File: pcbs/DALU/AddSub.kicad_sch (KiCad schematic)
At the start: 14 parts, among them U401 74HC86, U402 74HC08, U403 74HC86, U404 74HC86, U405 74HC283, U406 74HC283, U407 74HC245, U408 74HC245

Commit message: More rerouting
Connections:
- net RESULT7: now reaches U407.11 (B7)
- net RESULT6: now reaches U407.12 (B6)
- net RESULT5: now reaches U407.13 (B5)
- net RESULT4: now reaches U407.14 (B4)
- net RESULT3: now reaches U407.15 (B3)
- net RESULT2: now reaches U407.16 (B2)
- net RESULT1: now reaches U407.17 (B1)
- net RESULT0: now reaches U407.18 (B0)
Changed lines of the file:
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@@
+    (stroke (width 0) (type default) (color 0 0 0 0))
+  )
+  (bus_entry (at 254.635 43.18) (size -2.54 2.54)
     (stroke (width 0) (type default) (color 0 0 0 0))
   )
@@
     (stroke (width 0) (type default) (color 0 0 0 0))
   )
+  (bus_entry (at 254.635 50.8) (size -2.54 2.54)
+    (stroke (width 0) (type default) (color 0 0 0 0))
+  )
   (bus_entry (at 100.33 144.78) (size -2.54 2.54)
     (stroke (width 0) (type default) (color 0 0 0 0))
@@
     (stroke (width 0) (type default) (color 0 0 0 0))
   )
+  (bus_entry (at 254.635 55.88) (size -2.54 2.54)
+    (stroke (width 0) (type default) (color 0 0 0 0))
+  )
+  (bus_entry (at 254.635 45.72) (size -2.54 2.54)
+    (stroke (width 0) (type default) (color 0 0 0 0))
+  )
   (bus_entry (at 64.77 49.53) (size 2.54 2.54)
     (stroke (width 0) (type default) (color 0 0 0 0))
   )
+  (bus_entry (at 254.635 58.42) (size -2.54 2.54)
+    (stroke (width 0) (type default) (color 0 0 0 0))
+  )
   (bus_entry (at 64.77 96.52) (size 2.54 2.54)
     (stroke (width 0) (type default) (color 0 0 0 0))
@@
     (stroke (width 0) (type default) (color 0 0 0 0))
   )
+  (bus_entry (at 254.635 48.26) (size -2.54 2.54)
+    (stroke (width 0) (type default) (color 0 0 0 0))
+  )
   (bus_entry (at 100.33 114.3) (size -2.54 2.54)
     (stroke (width 0) (type default) (color 0 0 0 0))
@@
     (stroke (width 0) (type default) (color 0 0 0 0))
   )
+  (bus_entry (at 254.635 60.96) (size -2.54 2.54)
+    (stroke (width 0) (type default) (color 0 0 0 0))
+  )
   (bus_entry (at 134.62 63.5) (size 2.54 2.54)
     (stroke (width 0) (type default) (color 0 0 0 0))
@@
     (stroke (width 0) (type default) (color 0 0 0 0))
   )
+  (bus_entry (at 254.635 53.34) (size -2.54 2.54)
+    (stroke (width 0) (type default) (color 0 0 0 0))
+  )
   (bus_entry (at 143.51 55.88) (size 2.54 2.54)
     (stroke (width 0) (type default) (color 0 0 0 0))
@@
     (stroke (width 0) (type default) (color 0 0 0 0))
   )
+  (bus (pts (xy 254.635 36.83) (xy 254.635 43.18))
+    (stroke (width 0) (type default) (color 0 0 0 0))
+  )
   (wire (pts (xy 60.96 63.5) (xy 60.96 72.39))
     (stroke (width 0) (type default) (color 0 0 0 0))
@@
     (stroke (width 0) (type default) (color 0 0 0 0))
   )
+  (bus (pts (xy 254.635 43.18) (xy 254.635 45.72))
+    (stroke (width 0) (type default) (color 0 0 0 0))
+  )
   (wire (pts (xy 137.16 120.65) (xy 156.21 120.65))
     (stroke (width 0) (type default) (color 0 0 0 0))
@@
     (stroke (width 0) (type default) (color 0 0 0 0))
   )
+  (bus (pts (xy 254.635 58.42) (xy 254.635 60.96))
+    (stroke (width 0) (type default) (color 0 0 0 0))
+  )
   (wire (pts (xy 193.675 146.685) (xy 193.675 149.86))
     (stroke (width 0) (type default) (color 0 0 0 0))
   )
+  (bus (pts (xy 261.62 36.83) (xy 254.635 36.83))
+    (stroke (width 0) (type default) (color 0 0 0 0))
+  )
   (wire (pts (xy 163.83 87.63) (xy 168.91 87.63))
     (stroke (width 0) (type default) (color 0 0 0 0))
@@
     (stroke (width 0) (type default) (color 0 0 0 0))
   )
+  (bus (pts (xy 254.635 50.8) (xy 254.635 53.34))
+    (stroke (width 0) (type default) (color 0 0 0 0))
+  )
   (wire (pts (xy 227.33 120.65) (xy 232.41 120.65))
     (stroke (width 0) (type default) (color 0 0 0 0))
@@
     (stroke (width 0) (type default) (color 0 0 0 0))
   )
+  (bus (pts (xy 254.635 48.26) (xy 254.635 50.8))
+    (stroke (width 0) (type default) (color 0 0 0 0))
+  )
   (wire (pts (xy 163.83 78.74) (xy 168.91 78.74))
     (stroke (width 0) (type default) (color 0 0 0 0))
@@
     (stroke (width 0) (type default) (color 0 0 0 0))
   )
+  (wire (pts (xy 238.76 50.8) (xy 252.095 50.8))
+    (stroke (width 0) (type default) (color 0 0 0 0))
+  )
   (bus (pts (xy 134.62 113.03) (xy 134.62 110.49))
     (stroke (width 0) (type default) (color 0 0 0 0))
@@
     (stroke (width 0) (type default) (color 0 0 0 0))
   )
+  (bus (pts (xy 254.635 45.72) (xy 254.635 48.26))
+    (stroke (width 0) (type default) (color 0 0 0 0))
+  )
   (wire (pts (xy 67.31 36.83) (xy 77.47 36.83))
     (stroke (width 0) (type default) (color 0 0 0 0))
@@
     (stroke (width 0) (type default) (color 0 0 0 0))
   )
+  (wire (pts (xy 238.76 58.42) (xy 252.095 58.42))
+    (stroke (width 0) (type default) (color 0 0 0 0))
+  )
   (bus (pts (xy 143.51 53.34) (xy 143.51 55.88))
     (stroke (width 0) (type default) (color 0 0 0 0))
   )
+  (wire (pts (xy 238.76 55.88) (xy 252.095 55.88))
+    (stroke (width 0) (type default) (color 0 0 0 0))
+  )
   (wire (pts (xy 77.47 134.62) (xy 60.96 134.62))
     (stroke (width 0) (type default) (color 0 0 0 0))
@@
     (stroke (width 0) (type default) (color 0 0 0 0))
   )
+  (bus (pts (xy 254.635 55.88) (xy 254.635 58.42))
+    (stroke (width 0) (type default) (color 0 0 0 0))
+  )
+  (wire (pts (xy 238.76 63.5) (xy 252.095 63.5))
+    (stroke (width 0) (type default) (color 0 0 0 0))
+  )
   (wire (pts (xy 168.91 35.56) (xy 168.91 38.1))
     (stroke (width 0) (type default) (color 0 0 0 0))
@@
     (stroke (width 0) (type default) (color 0 0 0 0))
   )
+  (wire (pts (xy 238.76 45.72) (xy 252.095 45.72))
+    (stroke (width 0) (type default) (color 0 0 0 0))
+  )
   (wire (pts (xy 67.31 67.31) (xy 77.47 67.31))
     (stroke (width 0) (type default) (color 0 0 0 0))
@@
     (stroke (width 0) (type default) (color 0 0 0 0))
   )
+  (wire (pts (xy 238.76 48.26) (xy 252.095 48.26))
+    (stroke (width 0) (type default) (color 0 0 0 0))
+  )
   (bus (pts (xy 134.62 115.57) (xy 134.62 113.03))
     (stroke (width 0) (type default) (color 0 0 0 0))
@@
     (stroke (width 0) (type default) (color 0 0 0 0))
   )
+  (bus (pts (xy 254.635 53.34) (xy 254.635 55.88))
+    (stroke (width 0) (type default) (color 0 0 0 0))
+  )
   (bus (pts (xy 134.62 110.49) (xy 134.62 68.58))
     (stroke (width 0) (type default) (color 0 0 0 0))
@@
     (stroke (width 0) (type default) (color 0 0 0 0))
   )
+  (wire (pts (xy 238.76 60.96) (xy 252.095 60.96))
+    (stroke (width 0) (type default) (color 0 0 0 0))
+  )
   (wire (pts (xy 146.05 50.8) (xy 156.21 50.8))
     (stroke (width 0) (type default) (color 0 0 0 0))
@@
   )
   (wire (pts (xy 77.47 72.39) (xy 60.96 72.39))
+    (stroke (width 0) (type default) (color 0 0 0 0))
+  )
+  (wire (pts (xy 238.76 53.34) (xy 252.095 53.34))
     (stroke (width 0) (type default) (color 0 0 0 0))
   )
@@
     (effects (font (size 1.27 1.27)) (justify left bottom))
   )
+  (label "RESULT4" (at 238.76 55.88 0)
+    (effects (font (size 1.27 1.27)) (justify left bottom))
+  )
+  (label "RESULT3" (at 238.76 53.34 0)
+    (effects (font (size 1.27 1.27)) (justify left bottom))
+  )
   (label "B'4" (at 137.16 113.03 0)
     (effects (font (size 1.27 1.27)) (justify left bottom))
@@
     (effects (font (size 1.27 1.27)) (justify left bottom))
   )
+  (label "RESULT2" (at 238.76 50.8 0)
+    (effects (font (size 1.27 1.27)) (justify left bottom))
+  )
+  (label "RESULT5" (at 238.76 58.42 0)
+    (effects (font (size 1.27 1.27)) (justify left bottom))
+  )
   (label "B'0" (at 92.71 39.37 0)
     (effects (font (size 1.27 1.27)) (justify left bottom))
@@
     (effects (font (size 1.27 1.27)) (justify left bottom))
   )
+  (label "RESULT6" (at 238.76 60.96 0)
+    (effects (font (size 1.27 1.27)) (justify left bottom))
+  )
   (label "A5" (at 146.05 102.87 0)
     (effects (font (size 1.27 1.27)) (justify left bottom))
   )
   (label "S_{1}" (at 182.88 48.26 0)
+    (effects (font (size 1.27 1.27)) (justify left bottom))
+  )
+  (label "RESULT0" (at 238.76 45.72 0)
     (effects (font (size 1.27 1.27)) (justify left bottom))
   )
@@
     (effects (font (size 1.27 1.27)) (justify left bottom))
   )
+  (label "RESULT1" (at 238.76 48.26 0)
+    (effects (font (size 1.27 1.27)) (justify left bottom))
+  )
   (label "A0" (at 146.685 50.8 0)
     (effects (font (size 1.27 1.27)) (justify left bottom))
@@
   )
   (label "B'0" (at 137.16 63.5 0)
+    (effects (font (size 1.27 1.27)) (justify left bottom))
+  )
+  (label "RESULT7" (at 238.76 63.5 0)
     (effects (font (size 1.27 1.27)) (justify left bottom))
   )
@@
     (effects (font (size 1.27 1.27)) (justify right))
   )
+  (hierarchical_label "RESULT[0..7]" (shape tri_state) (at 261.62 36.83 0)
+    (effects (font (size 1.27 1.27)) (justify left))
+  )
   (hierarchical_label "B[0..7]" (shape input) (at 45.72 29.21 180)

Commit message: Finish preliminary routing
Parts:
- added C407, C408: 100n, Capacitor_SMD:C_0603_1608Metric, symbol Device:C
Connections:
- net +5V: now also C407.1, C408.1
- net GND: now also C407.2, C408.2
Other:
- moved on the sheet: C401, C402, C403, C404, C405, C406

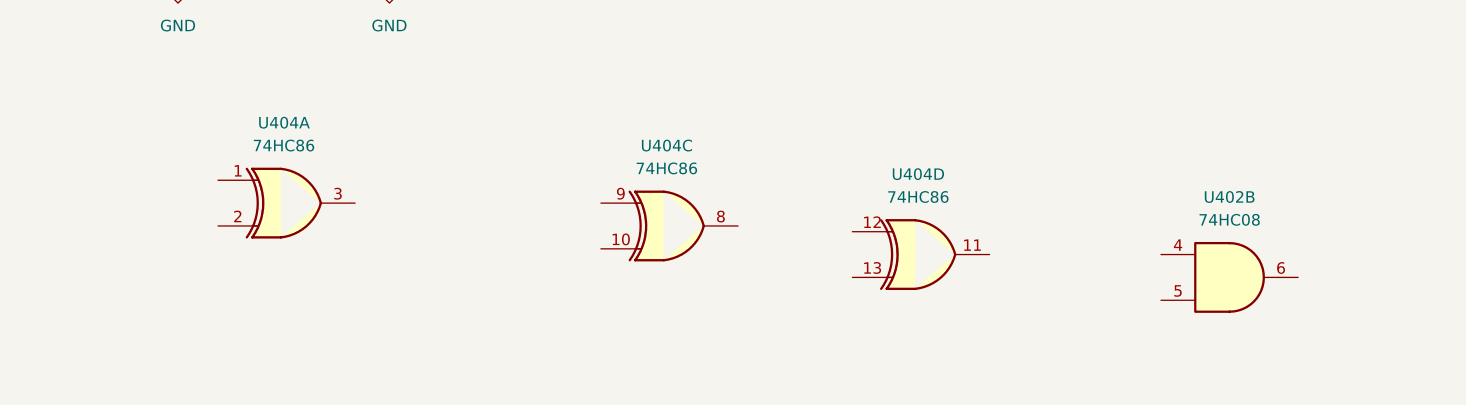
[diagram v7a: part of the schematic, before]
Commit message: Filling out connections
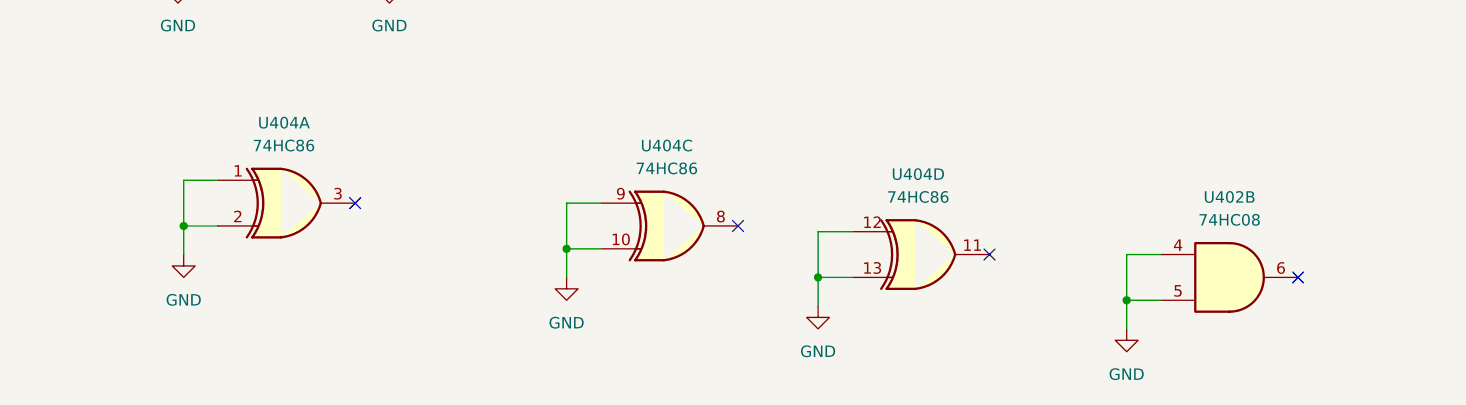
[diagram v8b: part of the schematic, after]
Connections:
- net GND: now also U402.4, U402.5, U404.1, U404.10, U404.12, U404.13, U404.2, U404.9
- no-connect marks 7 -> 11
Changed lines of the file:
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@@
   (junction (at 173.99 161.29) (diameter 0) (color 0 0 0 0)
   )
+  (junction (at 88.265 219.075) (diameter 0) (color 0 0 0 0)
+  )
   (junction (at 227.33 115.57) (diameter 0) (color 0 0 0 0)
   )
@@
   (junction (at 193.675 161.29) (diameter 0) (color 0 0 0 0)
   )
+  (junction (at 193.04 227.33) (diameter 0) (color 0 0 0 0)
+  )
   (junction (at 180.34 149.225) (diameter 0) (color 0 0 0 0)
   )
@@
   (junction (at 205.74 161.29) (diameter 0) (color 0 0 0 0)
   )
+  (junction (at 130.81 221.615) (diameter 0) (color 0 0 0 0)
+  )
   (junction (at 217.805 161.29) (diameter 0) (color 0 0 0 0)
   )
@@
   )
   (junction (at 60.96 127) (diameter 0) (color 0 0 0 0)
+  )
+  (junction (at 158.75 224.79) (diameter 0) (color 0 0 0 0)
   )
   (junction (at 231.14 149.225) (diameter 0) (color 0 0 0 0)
@@
   (no_connect (at 257.81 110.49))
   (no_connect (at 257.81 115.57))
+  (no_connect (at 212.09 224.79))
   (no_connect (at 257.81 113.03))
   (no_connect (at 257.81 118.11))
+  (no_connect (at 149.86 219.075))
+  (no_connect (at 107.315 216.535))
   (no_connect (at 257.81 107.95))
   (no_connect (at 257.81 120.65))
+  (no_connect (at 177.8 222.25))
   (bus_entry (at 100.33 52.07) (size -2.54 2.54)
     (stroke (width 0) (type default) (color 0 0 0 0))
@@
     (stroke (width 0) (type default) (color 0 0 0 0))
   )
+  (wire (pts (xy 88.265 222.25) (xy 88.265 219.075))
+    (stroke (width 0) (type default) (color 0 0 0 0))
+  )
   (wire (pts (xy 31.75 124.46) (xy 39.37 124.46))
     (stroke (width 0) (type default) (color 0 0 0 0))
   )
+  (wire (pts (xy 130.81 216.535) (xy 134.62 216.535))
+    (stroke (width 0) (type default) (color 0 0 0 0))
+  )
   (bus (pts (xy 134.62 66.04) (xy 134.62 63.5))
     (stroke (width 0) (type default) (color 0 0 0 0))
@@
     (stroke (width 0) (type default) (color 0 0 0 0))
   )
+  (wire (pts (xy 193.04 227.33) (xy 193.04 222.25))
+    (stroke (width 0) (type default) (color 0 0 0 0))
+  )
   (bus (pts (xy 254.635 58.42) (xy 254.635 60.96))
     (stroke (width 0) (type default) (color 0 0 0 0))
@@
     (stroke (width 0) (type default) (color 0 0 0 0))
   )
+  (wire (pts (xy 158.75 224.79) (xy 162.56 224.79))
+    (stroke (width 0) (type default) (color 0 0 0 0))
+  )
   (wire (pts (xy 146.05 105.41) (xy 156.21 105.41))
     (stroke (width 0) (type default) (color 0 0 0 0))
@@
     (stroke (width 0) (type default) (color 0 0 0 0))
   )
+  (wire (pts (xy 158.75 224.79) (xy 158.75 219.71))
+    (stroke (width 0) (type default) (color 0 0 0 0))
+  )
   (wire (pts (xy 67.31 144.78) (xy 77.47 144.78))
     (stroke (width 0) (type default) (color 0 0 0 0))
@@
     (stroke (width 0) (type default) (color 0 0 0 0))
   )
+  (wire (pts (xy 130.81 221.615) (xy 130.81 216.535))
+    (stroke (width 0) (type default) (color 0 0 0 0))
+  )
+  (wire (pts (xy 193.04 227.33) (xy 196.85 227.33))
+    (stroke (width 0) (type default) (color 0 0 0 0))
+  )
   (wire (pts (xy 77.47 57.15) (xy 60.96 57.15))
     (stroke (width 0) (type default) (color 0 0 0 0))
@@
     (stroke (width 0) (type default) (color 0 0 0 0))
   )
+  (wire (pts (xy 130.81 221.615) (xy 134.62 221.615))
+    (stroke (width 0) (type default) (color 0 0 0 0))
+  )
   (wire (pts (xy 67.31 67.31) (xy 77.47 67.31))
     (stroke (width 0) (type default) (color 0 0 0 0))
@@
     (stroke (width 0) (type default) (color 0 0 0 0))
   )
+  (wire (pts (xy 158.75 219.71) (xy 162.56 219.71))
+    (stroke (width 0) (type default) (color 0 0 0 0))
+  )
   (wire (pts (xy 181.61 48.26) (xy 213.36 48.26))
     (stroke (width 0) (type default) (color 0 0 0 0))
@@
     (stroke (width 0) (type default) (color 0 0 0 0))
   )
+  (wire (pts (xy 130.81 224.79) (xy 130.81 221.615))
+    (stroke (width 0) (type default) (color 0 0 0 0))
+  )
+  (wire (pts (xy 193.04 222.25) (xy 196.85 222.25))
+    (stroke (width 0) (type default) (color 0 0 0 0))
+  )
   (wire (pts (xy 186.69 58.42) (xy 186.69 82.55))
     (stroke (width 0) (type default) (color 0 0 0 0))
@@
     (stroke (width 0) (type default) (color 0 0 0 0))
   )
+  (wire (pts (xy 88.265 219.075) (xy 88.265 213.995))
+    (stroke (width 0) (type default) (color 0 0 0 0))
+  )
   (wire (pts (xy 227.33 113.03) (xy 232.41 113.03))
     (stroke (width 0) (type default) (color 0 0 0 0))
@@
     (stroke (width 0) (type default) (color 0 0 0 0))
   )
+  (wire (pts (xy 88.265 213.995) (xy 92.075 213.995))
+    (stroke (width 0) (type default) (color 0 0 0 0))
+  )
   (wire (pts (xy 205.74 149.225) (xy 205.74 152.4))
     (stroke (width 0) (type default) (color 0 0 0 0))
@@
     (stroke (width 0) (type default) (color 0 0 0 0))
   )
+  (wire (pts (xy 193.04 230.505) (xy 193.04 227.33))
+    (stroke (width 0) (type default) (color 0 0 0 0))
+  )
   (wire (pts (xy 33.02 60.96) (xy 40.64 60.96))
     (stroke (width 0) (type default) (color 0 0 0 0))
@@
     (stroke (width 0) (type default) (color 0 0 0 0))
   )
+  (wire (pts (xy 88.265 219.075) (xy 92.075 219.075))
+    (stroke (width 0) (type default) (color 0 0 0 0))
+  )
   (bus (pts (xy 64.77 29.21) (xy 64.77 34.29))
     (stroke (width 0) (type default) (color 0 0 0 0))
@@
   )
   (wire (pts (xy 238.76 60.96) (xy 252.095 60.96))
+    (stroke (width 0) (type default) (color 0 0 0 0))
+  )
+  (wire (pts (xy 158.75 227.965) (xy 158.75 224.79))
     (stroke (width 0) (type default) (color 0 0 0 0))
   )
@@
     )
     (property "Datasheet" "" (id 3) (at 173.99 161.29 0)
+      (effects (font (size 1.27 1.27)) hide)
+    )
+    (pin "1")
+  )
+  (symbol (lib_id "power:GND") (at 88.265 222.25 0) (unit 1)
+    (in_bom yes) (on_board yes) (fields_autoplaced)
+    (property "Reference" "#PWR0101" (id 0) (at 88.265 228.6 0)
+      (effects (font (size 1.27 1.27)) hide)
+    )
+    (property "Value" "GND" (id 1) (at 88.265 227.33 0))
+    (property "Footprint" "" (id 2) (at 88.265 222.25 0)
+      (effects (font (size 1.27 1.27)) hide)
+    )
+    (property "Datasheet" "" (id 3) (at 88.265 222.25 0)
       (effects (font (size 1.27 1.27)) hide)
     )
@@
     (pin "2")
   )
+  (symbol (lib_id "power:GND") (at 193.04 230.505 0) (unit 1)
+    (in_bom yes) (on_board yes) (fields_autoplaced)
+    (property "Reference" "#PWR0104" (id 0) (at 193.04 236.855 0)
+      (effects (font (size 1.27 1.27)) hide)
+    )
+    (property "Value" "GND" (id 1) (at 193.04 235.585 0))
+    (property "Footprint" "" (id 2) (at 193.04 230.505 0)
+      (effects (font (size 1.27 1.27)) hide)
+    )
+    (property "Datasheet" "" (id 3) (at 193.04 230.505 0)
+      (effects (font (size 1.27 1.27)) hide)
+    )
+    (pin "1")
+  )
   (symbol (lib_id "power:GND") (at 224.79 123.19 270) (unit 1)
     (in_bom yes) (on_board yes) (fields_autoplaced)
@@
     (pin "7")
   )
+  (symbol (lib_id "power:GND") (at 130.81 224.79 0) (unit 1)
+    (in_bom yes) (on_board yes) (fields_autoplaced)
+    (property "Reference" "#PWR0102" (id 0) (at 130.81 231.14 0)
+      (effects (font (size 1.27 1.27)) hide)
+    )
+    (property "Value" "GND" (id 1) (at 130.81 229.87 0))
+    (property "Footprint" "" (id 2) (at 130.81 224.79 0)
+      (effects (font (size 1.27 1.27)) hide)
+    )
+    (property "Datasheet" "" (id 3) (at 130.81 224.79 0)
+      (effects (font (size 1.27 1.27)) hide)
+    )
+    (pin "1")
+  )
   (symbol (lib_id "74xx:74LS283") (at 168.91 107.95 0) (unit 1)
     (in_bom yes) (on_board yes) (fields_autoplaced)
@@
     (pin "7")
   )
+  (symbol (lib_id "power:GND") (at 158.75 227.965 0) (unit 1)
+    (in_bom yes) (on_board yes) (fields_autoplaced)
+    (property "Reference" "#PWR0103" (id 0) (at 158.75 234.315 0)
+      (effects (font (size 1.27 1.27)) hide)
+    )
+    (property "Value" "GND" (id 1) (at 158.75 233.045 0))
+    (property "Footprint" "" (id 2) (at 158.75 227.965 0)
+      (effects (font (size 1.27 1.27)) hide)
+    )
+    (property "Datasheet" "" (id 3) (at 158.75 227.965 0)
+      (effects (font (size 1.27 1.27)) hide)
+    )
+    (pin "1")
+  )
   (symbol (lib_id "74xx:74HC86") (at 85.09 54.61 0) (unit 2)
